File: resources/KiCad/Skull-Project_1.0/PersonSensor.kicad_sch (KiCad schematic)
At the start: 5 parts, among them U1 RS_FlipFlop_Dual_14P

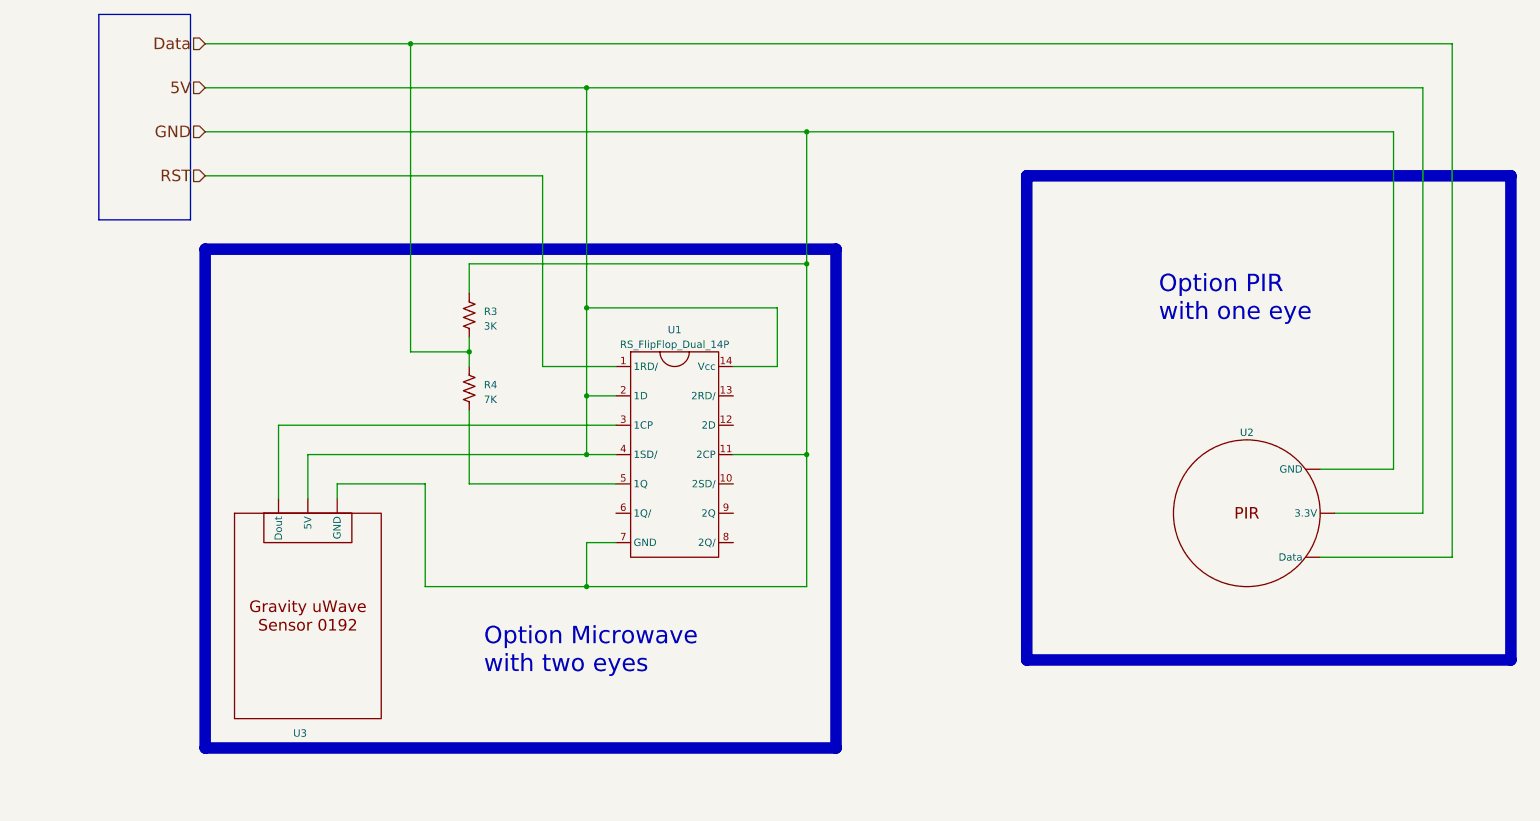
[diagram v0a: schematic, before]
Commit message: clean up schematic
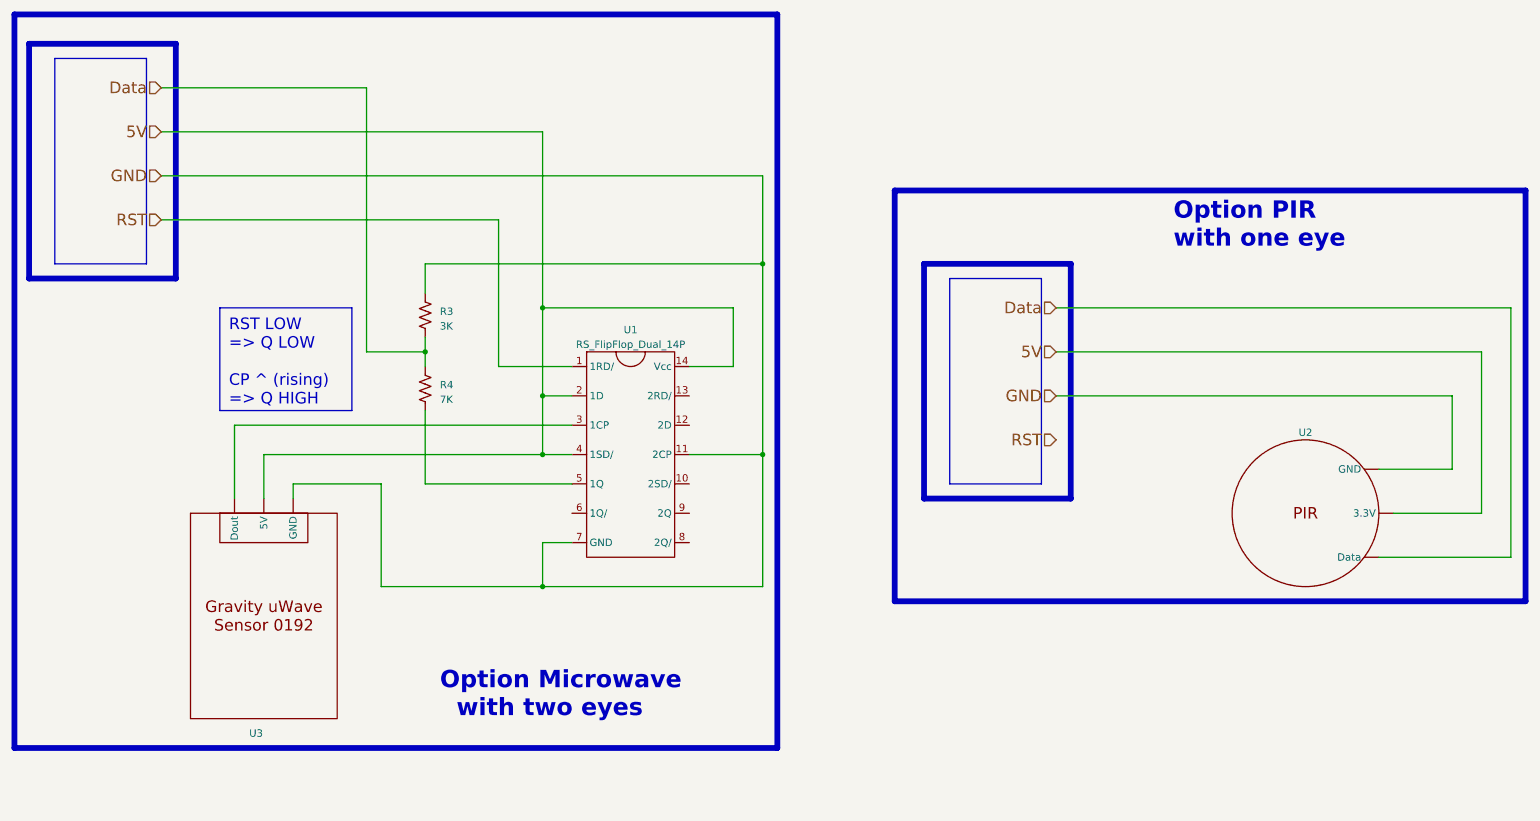
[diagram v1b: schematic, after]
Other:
- moved on the sheet: R3, R4, U1, U2, U3

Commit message: microwave sensor now uses NANO for edge detect
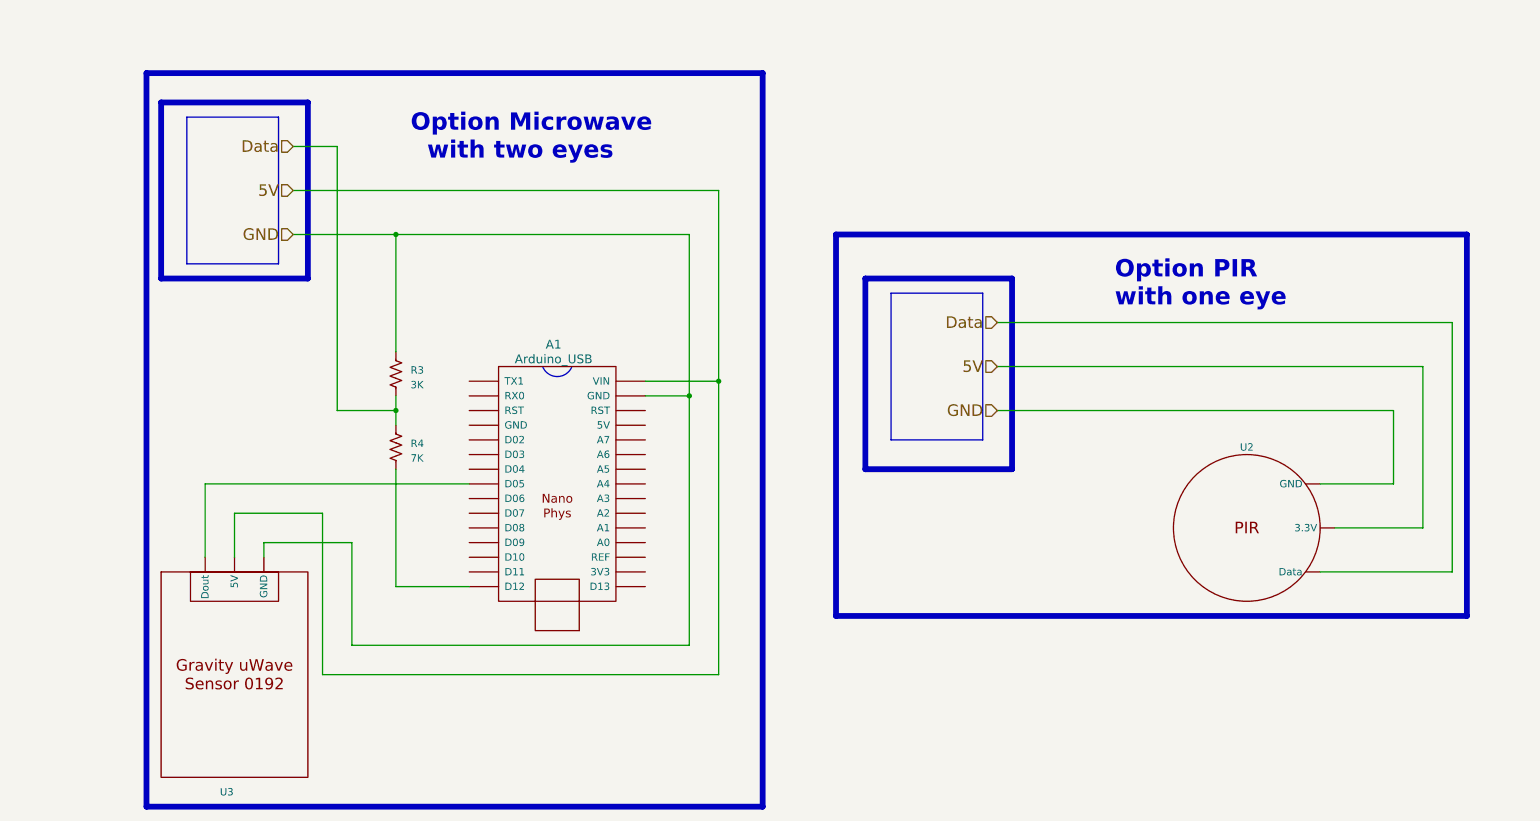
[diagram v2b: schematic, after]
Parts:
- removed U1: RS_FlipFlop_Dual_14P, symbol mdoLibrary:RS_FlipFlop_Dual_14P
- added A1: Arduino_USB, symbol mdoLibrary:Arduino_USB
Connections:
- net 5V : now also A1.~ (VIN)
- net GND : now also A1.~ (VIN)
- net at R4.2: now also A1.~ (VIN)
- new net: A1.~ (VIN), U3. (GND)
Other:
- moved on the sheet: R3, R4, U2, U3

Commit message: microwave sensor now uses NANO for edge detect
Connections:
- new net: A1.~ (VIN), U3. (GND)

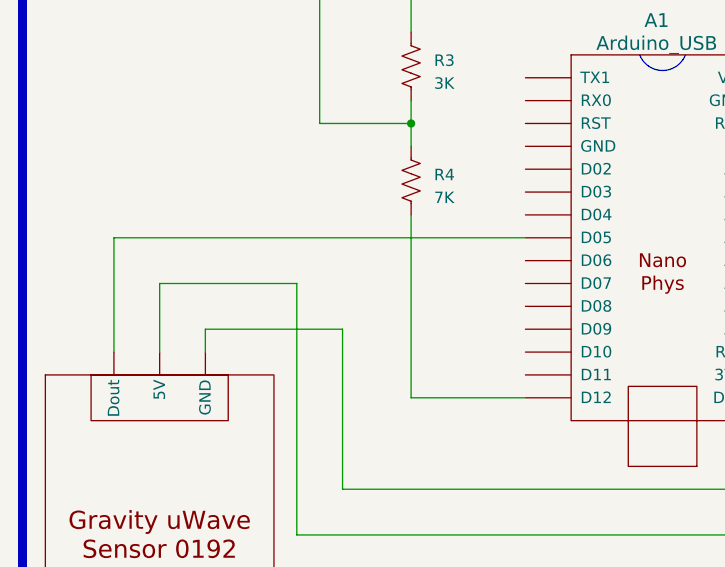
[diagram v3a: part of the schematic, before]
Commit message: schematic update pin on NANO
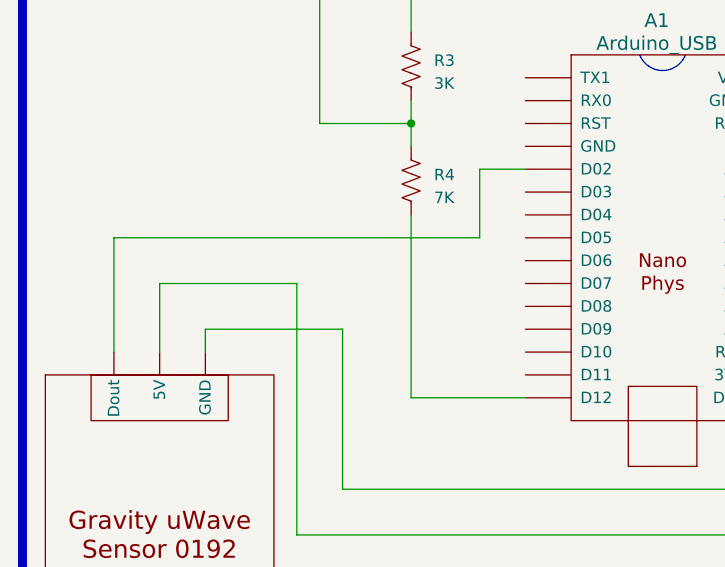
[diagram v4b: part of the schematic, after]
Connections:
- new net: A1.~ (VIN), U3. (GND)
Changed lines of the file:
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@@
   (junction (at 134.62 81.28) (diameter 0) (color 0 0 0 0)
-  )
-  (wire (pts (xy 96.52 96.52) (xy 50.8 96.52))
-    (stroke (width 0) (type default))
   )
   (wire (pts (xy 134.62 81.28) (xy 134.62 124.46))
@@
   )
   (wire (pts (xy 71.12 129.54) (xy 71.12 101.6))
+    (stroke (width 0) (type default))
+  )
+  (wire (pts (xy 96.52 88.9) (xy 91.44 88.9))
     (stroke (width 0) (type default))
   )
@@
     (stroke (width 0) (type default))
   )
+  (wire (pts (xy 91.44 88.9) (xy 91.44 96.52))
+    (stroke (width 0) (type default))
+  )
   (wire (pts (xy 83.82 53.34) (xy 83.82 73.66))
+    (stroke (width 0) (type default))
+  )
+  (wire (pts (xy 83.82 114.3) (xy 96.52 114.3))
     (stroke (width 0) (type default))
   )
@@
   )
   (wire (pts (xy 83.82 93.98) (xy 83.82 114.3))
-    (stroke (width 0) (type default))
-  )
-  (wire (pts (xy 96.52 114.3) (xy 83.82 114.3))
     (stroke (width 0) (type default))
   )
@@
     (stroke (width 0) (type default))
   )
+  (wire (pts (xy 91.44 96.52) (xy 50.8 96.52))
+    (stroke (width 0) (type default))
+  )

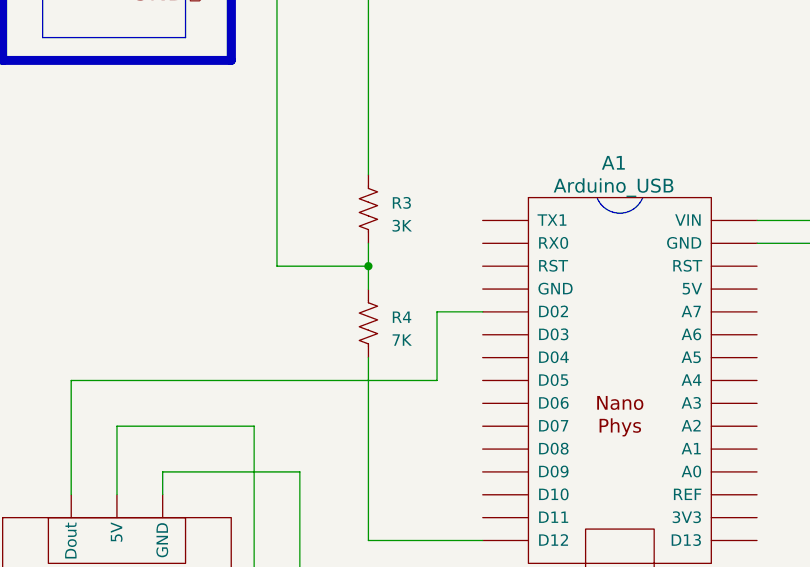
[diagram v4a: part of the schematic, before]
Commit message: correct schematic 3K/7K resistors
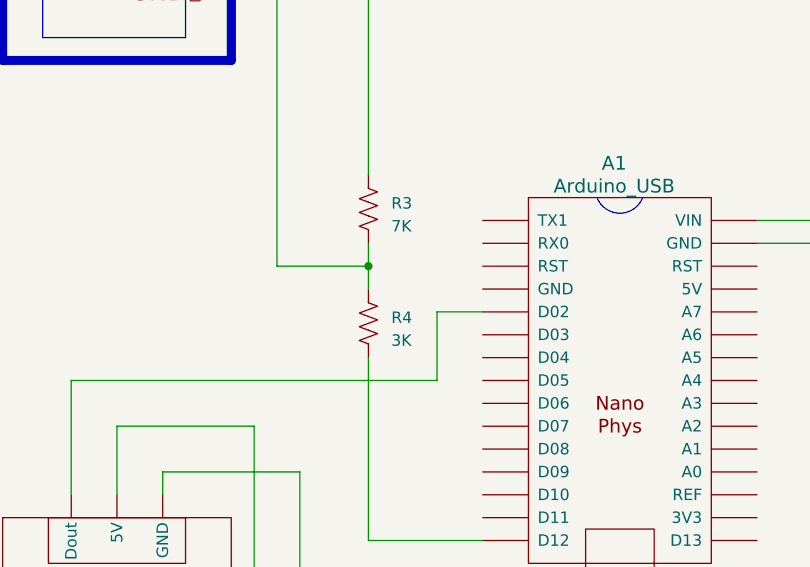
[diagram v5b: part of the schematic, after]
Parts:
- R3: value 3K -> 7K
- R4: value 7K -> 3K
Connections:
- new net: A1.~ (VIN), U3. (GND)
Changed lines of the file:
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@@
       (effects (font (size 1.27 1.27)) (justify left))
     )
-    (property "Value" "7K" (at 86.36 92.075 0)
+    (property "Value" "3K" (at 86.36 92.075 0)
       (effects (font (size 1.27 1.27)) (justify left))
     )
@@
       (effects (font (size 1.27 1.27)) (justify left))
     )
-    (property "Value" "3K" (at 86.36 79.375 0)
+    (property "Value" "7K" (at 86.36 79.375 0)
       (effects (font (size 1.27 1.27)) (justify left))
     )

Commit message: add wire colors to schematic
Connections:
- new net: A1.~ (VIN), U3. (GND)
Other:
- note added: "Black"
- note added: "Green"
- note added: "Red"
- note added: "White"
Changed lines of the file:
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@@
   (title_block
     (title "Skull-Project 1.0")
-    (date "2024-09-19")
+    (date "2024-09-20")
     (rev "1.0")
     (company "github.com/Mark-MDO47/Skull-Project")
@@
     (fill (type none))
   )
+  (text "White" (at 195.58 68.58 0)
+    (effects (font (size 1.27 1.27) bold) (justify left bottom))
+  )
+  (text "Red" (at 139.7 91.44 0)
+    (effects (font (size 1.27 1.27) bold) (justify left bottom))
+  )
+  (text "Black" (at 127 53.34 0)
+    (effects (font (size 1.27 1.27) bold) (justify left bottom))
+  )
+  (text "White" (at 243.84 111.76 0)
+    (effects (font (size 1.27 1.27) bold) (justify left bottom))
+  )
+  (text "Red" (at 127 45.72 0)
+    (effects (font (size 1.27 1.27) bold) (justify left bottom))
+  )
+  (text "Green" (at 50.8 96.52 0)
+    (effects (font (size 1.27 1.27) (thickness 0.254) bold) (justify left bottom))
+  )
   (text "Option Microwave\n  with two eyes" (at 86.36 40.64 0)
     (effects (font (size 3 3) (thickness 0.6) bold) (justify left bottom))
   )
+  (text "Black" (at 195.58 83.82 0)
+    (effects (font (size 1.27 1.27) bold) (justify left bottom))
+  )
+  (text "White" (at 76.2 83.82 0)
+    (effects (font (size 1.27 1.27) bold) (justify left bottom))
+  )
+  (text "Black" (at 243.84 96.52 0)
+    (effects (font (size 1.27 1.27) bold) (justify left bottom))
+  )
+  (text "Red" (at 195.58 76.2 0)
+    (effects (font (size 1.27 1.27) bold) (justify left bottom))
+  )
+  (text "Black" (at 63.5 106.68 0)
+    (effects (font (size 1.27 1.27) bold) (justify left bottom))
+  )
+  (text "White" (at 76.2 38.1 0)
+    (effects (font (size 1.27 1.27) bold) (justify left bottom))
+  )
+  (text "Red" (at 243.84 104.14 0)
+    (effects (font (size 1.27 1.27) bold) (justify left bottom))
+  )
+  (text "Red" (at 76.2 45.72 0)
+    (effects (font (size 1.27 1.27) bold) (justify left bottom))
+  )
+  (text "Black" (at 134.62 88.9 0)
+    (effects (font (size 1.27 1.27) bold) (justify left bottom))
+  )
+  (text "Black" (at 83.82 63.5 0)
+    (effects (font (size 1.27 1.27) bold) (justify left bottom))
+  )
+  (text "Green" (at 86.36 99.06 0)
+    (effects (font (size 1.27 1.27) (thickness 0.254) bold) (justify left bottom))
+  )
   (text "Option PIR\nwith one eye" (at 208.28 66.04 0)
     (effects (font (size 3 3) (thickness 0.6) bold) (justify left bottom))
   )
+  (text "White" (at 86.36 114.3 0)
+    (effects (font (size 1.27 1.27) bold) (justify left bottom))
+  )
+  (text "Black" (at 91.44 124.46 0)
+    (effects (font (size 1.27 1.27) bold) (justify left bottom))
+  )
+  (text "Red" (at 63.5 101.6 0)
+    (effects (font (size 1.27 1.27) bold) (justify left bottom))
+  )
+  (text "Red" (at 91.44 129.54 0)
+    (effects (font (size 1.27 1.27) bold) (justify left bottom))
+  )
+  (text "Black" (at 76.2 53.34 0)
+    (effects (font (size 1.27 1.27) bold) (justify left bottom))
+  )
   (hierarchical_label "GND " (shape input) (at 187.96 83.82 180) (fields_autoplaced)

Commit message: schematic uses 4pin cable for power, details on internal skull cabling
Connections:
- new net: A1.~ (VIN), U3. (GND)
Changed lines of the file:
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@@
   (title_block
     (title "Skull-Project 1.0")
-    (date "2024-09-20")
+    (date "2024-09-25")
     (rev "1.0")
     (company "github.com/Mark-MDO47/Skull-Project")

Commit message: add rst-2-prim to schematic
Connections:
- new net: A1.~ (VIN), U3. (GND)
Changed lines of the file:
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@@
   (title_block
     (title "Skull-Project 1.0")
-    (date "2024-09-25")
+    (date "2024-09-27")
     (rev "1.0")
     (company "github.com/Mark-MDO47/Skull-Project")
